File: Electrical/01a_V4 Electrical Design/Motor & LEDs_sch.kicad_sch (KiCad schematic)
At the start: 18 parts, among them J21 B2B-PH-SM4-TB(LF)(SN), J4 B2B-PH-SM4-TB(LF)(SN), J5 SSM-103-F-SV-P-TR, J6 1x2 5mm screw terminal, J7 B4B-XH-A(LF)(SN), Q2 IRLML2502TRPBF

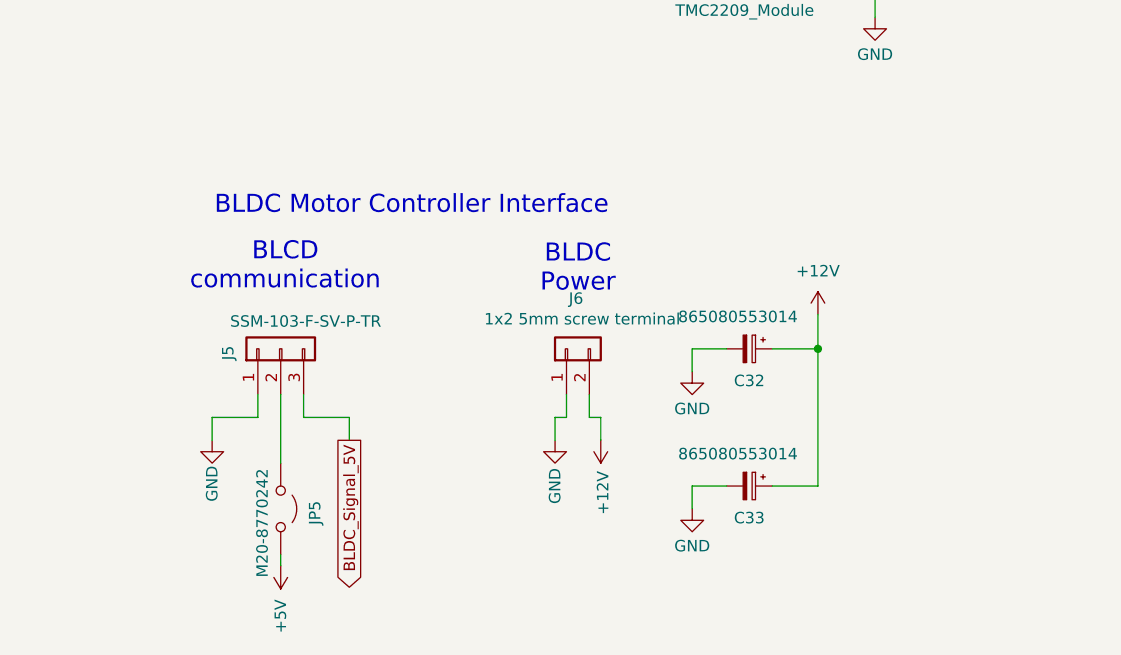
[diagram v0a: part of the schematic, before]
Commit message: adding LED Blade for Powered Platter 2. PCBs are being milled, 3D print needs to still be designed
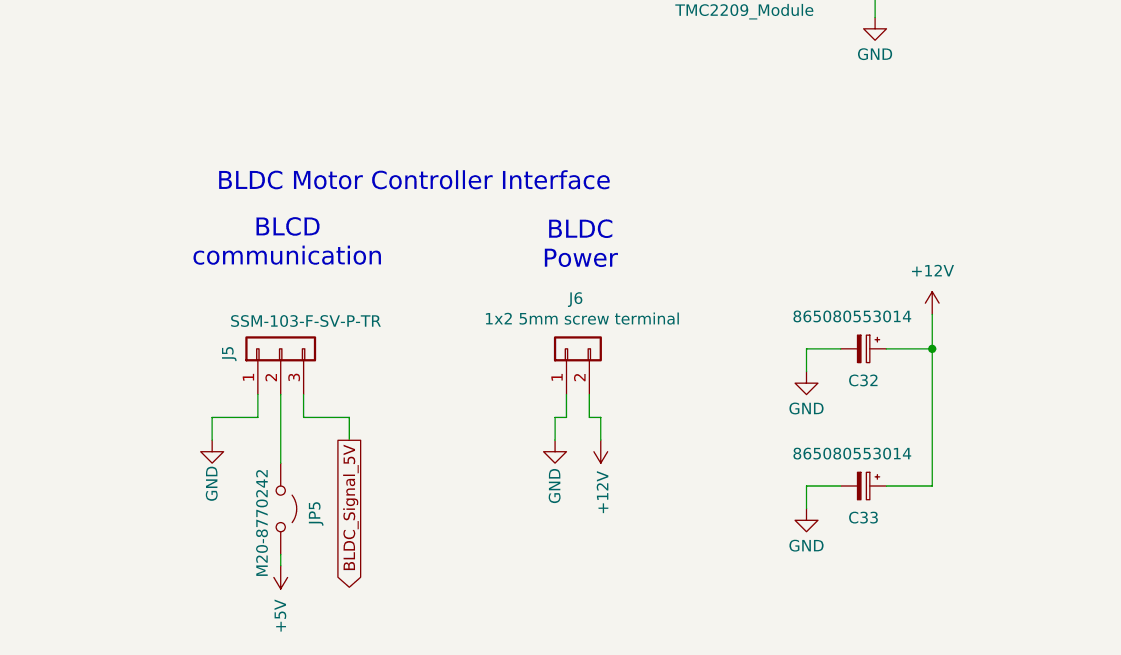
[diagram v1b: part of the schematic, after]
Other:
- moved on the sheet: C32, C33
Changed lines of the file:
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@@
 	(text "BLDC Motor Controller Interface"
 		(exclude_from_sim no)
-		(at 72.644 119.888 0)
+		(at 72.898 117.348 0)
 		(effects
 			(font
@@
 	(text "BLDC\nPower"
 		(exclude_from_sim no)
-		(at 113.03 128.524 0)
+		(at 113.284 125.984 0)
 		(effects
 			(font
@@
 	(text "BLCD\ncommunication"
 		(exclude_from_sim no)
-		(at 80.518 128.27 0)
+		(at 80.772 125.73 0)
 		(effects
 			(font
@@
 	)
 	(junction
-		(at 139.7 134.62)
+		(at 152.4 134.62)
 		(diameter 0)
 		(color 0 0 0 0)
@@
 	(wire
 		(pts
-			(xy 125.73 149.86) (xy 125.73 152.4)
+			(xy 138.43 149.86) (xy 138.43 152.4)
 		)
 		(stroke
@@
 	(wire
 		(pts
-			(xy 129.54 149.86) (xy 125.73 149.86)
+			(xy 142.24 149.86) (xy 138.43 149.86)
 		)
 		(stroke
@@
 	(wire
 		(pts
-			(xy 125.73 134.62) (xy 125.73 137.16)
+			(xy 138.43 134.62) (xy 138.43 137.16)
 		)
 		(stroke
@@
 	(wire
 		(pts
-			(xy 129.54 134.62) (xy 125.73 134.62)
+			(xy 142.24 134.62) (xy 138.43 134.62)
 		)
 		(stroke
@@
 	(wire
 		(pts
-			(xy 134.62 134.62) (xy 139.7 134.62)
+			(xy 147.32 134.62) (xy 152.4 134.62)
 		)
 		(stroke
@@
 	(wire
 		(pts
-			(xy 139.7 134.62) (xy 139.7 149.86)
+			(xy 152.4 134.62) (xy 152.4 149.86)
 		)
 		(stroke
@@
 	(wire
 		(pts
-			(xy 134.62 149.86) (xy 139.7 149.86)
+			(xy 147.32 149.86) (xy 152.4 149.86)
 		)
 		(stroke
@@
 	(wire
 		(pts
-			(xy 139.7 134.62) (xy 139.7 130.81)
+			(xy 152.4 134.62) (xy 152.4 130.81)
 		)
 		(stroke
@@
 	(symbol
 		(lib_id "Device:C_Polarized_Small")
-		(at 132.08 149.86 270)
+		(at 144.78 149.86 270)
 		(unit 1)
 		(body_style 1)
@@
 		(dnp no)
 		(property "Reference" "C33"
-			(at 132.08 153.416 90)
+			(at 144.78 153.416 90)
 			(show_name no)
 			(do_not_autoplace no)
@@
 		)
 		(property "Value" "865080553014"
-			(at 130.81 146.304 90)
+			(at 143.51 146.304 90)
 			(show_name no)
 			(do_not_autoplace no)
@@
 		)
 		(property "Footprint" "Footprint drive Dump 1:865080553014"
-			(at 132.08 149.86 0)
+			(at 144.78 149.86 0)
 			(hide yes)
 			(show_name no)
@@
 		)
 		(property "Datasheet" ""
-			(at 132.08 149.86 0)
+			(at 144.78 149.86 0)
 			(hide yes)
 			(show_name no)
@@
 		)
 		(property "Description" "Polarized capacitor, small symbol"
-			(at 132.08 149.86 0)
+			(at 144.78 149.86 0)
 			(hide yes)
 			(show_name no)
@@
 	(symbol
 		(lib_id "power:+12V")
-		(at 139.7 130.81 0)
+		(at 152.4 130.81 0)
 		(unit 1)
 		(body_style 1)
@@
 		(dnp no)
 		(property "Reference" "#PWR0186"
-			(at 139.7 134.62 0)
+			(at 152.4 134.62 0)
 			(hide yes)
 			(show_name no)
@@
 		)
 		(property "Value" "+12V"
-			(at 139.7 125.984 0)
+			(at 152.4 125.984 0)
 			(show_name no)
 			(do_not_autoplace no)
@@
 		)
 		(property "Footprint" ""
-			(at 139.7 130.81 0)
+			(at 152.4 130.81 0)
 			(hide yes)
 			(show_name no)
@@
 		)
 		(property "Datasheet" ""
-			(at 139.7 130.81 0)
+			(at 152.4 130.81 0)
 			(hide yes)
 			(show_name no)
@@
 		)
 		(property "Description" "Power symbol creates a global label with name \"+12V\""
-			(at 139.7 130.81 0)
+			(at 152.4 130.81 0)
 			(hide yes)
 			(show_name no)
@@
 		(lib_name "GND_1")
 		(lib_id "power:GND")
-		(at 125.73 152.4 0)
+		(at 138.43 152.4 0)
 		(unit 1)
 		(body_style 1)
@@
 		(fields_autoplaced yes)
 		(property "Reference" "#PWR0184"
-			(at 125.73 158.75 0)
+			(at 138.43 158.75 0)
 			(hide yes)
 			(show_name no)
@@
 		)
 		(property "Value" "GND"
-			(at 125.73 156.5331 0)
+			(at 138.43 156.5331 0)
 			(show_name no)
 			(do_not_autoplace no)
@@
 		)
 		(property "Footprint" ""
-			(at 125.73 152.4 0)
+			(at 138.43 152.4 0)
 			(hide yes)
 			(show_name no)
@@
 		)
 		(property "Datasheet" ""
-			(at 125.73 152.4 0)
+			(at 138.43 152.4 0)
 			(hide yes)
 			(show_name no)
@@
 		)
 		(property "Description" "Power symbol creates a global label with name \"GND\" , ground"
-			(at 125.73 152.4 0)
+			(at 138.43 152.4 0)
 			(hide yes)
 			(show_name no)
@@
 		(lib_name "GND_1")
 		(lib_id "power:GND")
-		(at 125.73 137.16 0)
+		(at 138.43 137.16 0)
 		(unit 1)
 		(body_style 1)
@@
 		(fields_autoplaced yes)
 		(property "Reference" "#PWR0182"
-			(at 125.73 143.51 0)
+			(at 138.43 143.51 0)
 			(hide yes)
 			(show_name no)
@@
 		)
 		(property "Value" "GND"
-			(at 125.73 141.2931 0)
+			(at 138.43 141.2931 0)
 			(show_name no)
 			(do_not_autoplace no)
@@
 		)
 		(property "Footprint" ""
-			(at 125.73 137.16 0)
+			(at 138.43 137.16 0)
 			(hide yes)
 			(show_name no)
@@
 		)
 		(property "Datasheet" ""
-			(at 125.73 137.16 0)
+			(at 138.43 137.16 0)
 			(hide yes)
 			(show_name no)
@@
 		)
 		(property "Description" "Power symbol creates a global label with name \"GND\" , ground"
-			(at 125.73 137.16 0)
+			(at 138.43 137.16 0)
 			(hide yes)
 			(show_name no)
@@
 	(symbol
 		(lib_id "Device:C_Polarized_Small")
-		(at 132.08 134.62 270)
+		(at 144.78 134.62 270)
 		(unit 1)
 		(body_style 1)
@@
 		(dnp no)
 		(property "Reference" "C32"
-			(at 132.08 138.176 90)
+			(at 144.78 138.176 90)
 			(show_name no)
 			(do_not_autoplace no)
@@
 		)
 		(property "Value" "865080553014"
-			(at 130.81 131.064 90)
+			(at 143.51 131.064 90)
 			(show_name no)
 			(do_not_autoplace no)
@@
 		)
 		(property "Footprint" "Footprint drive Dump 1:865080553014"
-			(at 132.08 134.62 0)
+			(at 144.78 134.62 0)
 			(hide yes)
 			(show_name no)
@@
 		)
 		(property "Datasheet" ""
-			(at 132.08 134.62 0)
+			(at 144.78 134.62 0)
 			(hide yes)
 			(show_name no)
@@
 		)
 		(property "Description" "Polarized capacitor, small symbol"
-			(at 132.08 134.62 0)
+			(at 144.78 134.62 0)
 			(hide yes)
 			(show_name no)
